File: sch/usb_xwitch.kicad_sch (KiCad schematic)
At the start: 82 parts, among them J1 USB3_A, J2 USB3_A, J3 USB3_A, J4 USB3_A, J5 USB3_A, J6 USB3_A, J7 Raspberry_Pi_2_3, J8 Conn_01x03, J9 Conn_02x03_Odd_Even, K1 J104D2C3VDC.15S, K2 J104D2C3VDC.15S, Q1 2N7002P, Q2 2N7002P, SW1 SW_MEC_5E, SW2 SW_MEC_5E, U1 Pico

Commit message: updated sch with correct lib
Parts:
- MUX1, MUX2: footprint USB_MUX_DEMUX_PI3USB302-A:USB_MUX_DEMUX_PI3USB302-A -> usb_xwitch:USB_MUX_DEMUX_PI3USB302-A
- U1: footprint RPi_Pico:RPi_Pico_SMD_TH -> usb_xwitch:RPi_Pico_SMD_TH
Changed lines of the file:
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@@
       (effects (font (size 1.27 1.27)) (justify left))
     )
-    (property "Footprint" "USB_MUX_DEMUX_PI3USB302-A:USB_MUX_DEMUX_PI3USB302-A" (id 2) (at 67.31 170.18 0)
+    (property "Footprint" "usb_xwitch:USB_MUX_DEMUX_PI3USB302-A" (id 2) (at 67.31 170.18 0)
       (effects (font (size 1.27 1.27)) hide)
     )
@@
       (effects (font (size 1.27 1.27)) (justify left))
     )
-    (property "Footprint" "USB_MUX_DEMUX_PI3USB302-A:USB_MUX_DEMUX_PI3USB302-A" (id 2) (at 139.7 62.23 0)
+    (property "Footprint" "usb_xwitch:USB_MUX_DEMUX_PI3USB302-A" (id 2) (at 139.7 62.23 0)
       (effects (font (size 1.27 1.27)) hide)
     )
@@
     (property "Reference" "U1" (id 0) (at 43.18 13.97 0))
     (property "Value" "Pico" (id 1) (at 43.18 16.51 0))
-    (property "Footprint" "RPi_Pico:RPi_Pico_SMD_TH" (id 2) (at 43.18 44.45 90)
+    (property "Footprint" "usb_xwitch:RPi_Pico_SMD_TH" (id 2) (at 43.18 44.45 90)
       (effects (font (size 1.27 1.27)) hide)
     )
@@
     )
     (path "/591ecbed-217e-48ed-ad79-2bef374432df"
-      (reference "MUX1") (unit 1) (value "PI3USB302-A") (footprint "USB_MUX_DEMUX_PI3USB302-A:USB_MUX_DEMUX_PI3USB302-A")
+      (reference "MUX1") (unit 1) (value "PI3USB302-A") (footprint "usb_xwitch:USB_MUX_DEMUX_PI3USB302-A")
     )
     (path "/32a0585d-b8a6-4ddd-ad0e-d8f7fa0d88f7"
-      (reference "MUX2") (unit 1) (value "PI3USB302-A") (footprint "USB_MUX_DEMUX_PI3USB302-A:USB_MUX_DEMUX_PI3USB302-A")
+      (reference "MUX2") (unit 1) (value "PI3USB302-A") (footprint "usb_xwitch:USB_MUX_DEMUX_PI3USB302-A")
     )
     (path "/01138bf6-010a-460b-9d5e-319df576379b"
@@
     )
     (path "/bb6a880b-1e04-4964-aba7-0ed014109109"
-      (reference "U1") (unit 1) (value "Pico") (footprint "RPi_Pico:RPi_Pico_SMD_TH")
-    )
-  )
+      (reference "U1") (unit 1) (value "Pico") (footprint "usb_xwitch:RPi_Pico_SMD_TH")
+    )
+  )

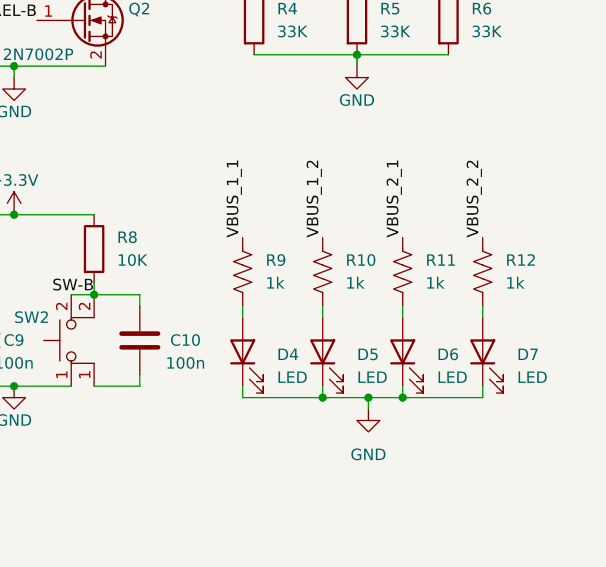
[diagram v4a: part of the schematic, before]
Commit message: updated led resistor value
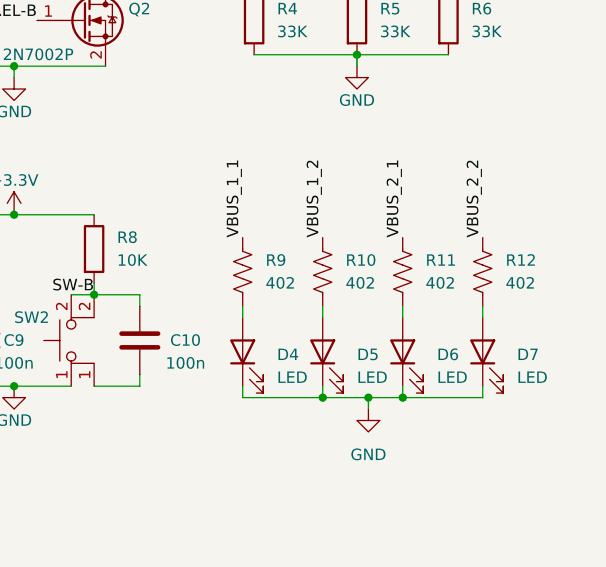
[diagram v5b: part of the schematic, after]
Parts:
- R10, R11, R12, R9: value 1k -> 402
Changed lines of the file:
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@@
       (effects (font (size 1.27 1.27)) (justify left))
     )
-    (property "Value" "1k" (id 1) (at 254 143.5099 0)
+    (property "Value" "402" (id 1) (at 254 143.5099 0)
       (effects (font (size 1.27 1.27)) (justify left))
     )
@@
       (effects (font (size 1.27 1.27)) (justify left))
     )
-    (property "Value" "1k" (id 1) (at 262.89 143.5099 0)
+    (property "Value" "402" (id 1) (at 262.89 143.5099 0)
       (effects (font (size 1.27 1.27)) (justify left))
     )
@@
       (effects (font (size 1.27 1.27)) (justify left))
     )
-    (property "Value" "1k" (id 1) (at 245.11 143.5099 0)
+    (property "Value" "402" (id 1) (at 245.11 143.5099 0)
       (effects (font (size 1.27 1.27)) (justify left))
     )
@@
       (effects (font (size 1.27 1.27)) (justify left))
     )
-    (property "Value" "1k" (id 1) (at 271.78 143.5099 0)
+    (property "Value" "402" (id 1) (at 271.78 143.5099 0)
       (effects (font (size 1.27 1.27)) (justify left))
     )
@@
     )
     (path "/ab7d4282-2b8b-4740-9065-f14f397a74b9"
-      (reference "R9") (unit 1) (value "1k") (footprint "Diode_SMD:D_0201_0603Metric_Pad0.64x0.40mm_HandSolder")
+      (reference "R9") (unit 1) (value "402") (footprint "Diode_SMD:D_0201_0603Metric_Pad0.64x0.40mm_HandSolder")
     )
     (path "/2077c3fe-878a-4115-9c7a-2c8d1e775f8e"
-      (reference "R10") (unit 1) (value "1k") (footprint "Diode_SMD:D_0201_0603Metric_Pad0.64x0.40mm_HandSolder")
+      (reference "R10") (unit 1) (value "402") (footprint "Diode_SMD:D_0201_0603Metric_Pad0.64x0.40mm_HandSolder")
     )
     (path "/61fa168a-7cd2-49f5-bf3a-d81e261300ae"
-      (reference "R11") (unit 1) (value "1k") (footprint "Diode_SMD:D_0201_0603Metric_Pad0.64x0.40mm_HandSolder")
+      (reference "R11") (unit 1) (value "402") (footprint "Diode_SMD:D_0201_0603Metric_Pad0.64x0.40mm_HandSolder")
     )
     (path "/ef6cee14-a255-4a4a-a342-1e947e99208d"
-      (reference "R12") (unit 1) (value "1k") (footprint "Diode_SMD:D_0201_0603Metric_Pad0.64x0.40mm_HandSolder")
+      (reference "R12") (unit 1) (value "402") (footprint "Diode_SMD:D_0201_0603Metric_Pad0.64x0.40mm_HandSolder")
     )
     (path "/e763556c-3aa8-4eb1-b263-7f108caa2254"

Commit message: updated pcb and sch
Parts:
- TP1, TP10, TP11, TP12, TP13, TP14, TP15, TP16, TP17, TP18, TP2, TP3, TP4, TP5, TP6, TP7, TP8, TP9: footprint TestPoint:TestPoint_Pad_D1.5mm -> TestPoint:TestPoint_Pad_D1.0mm

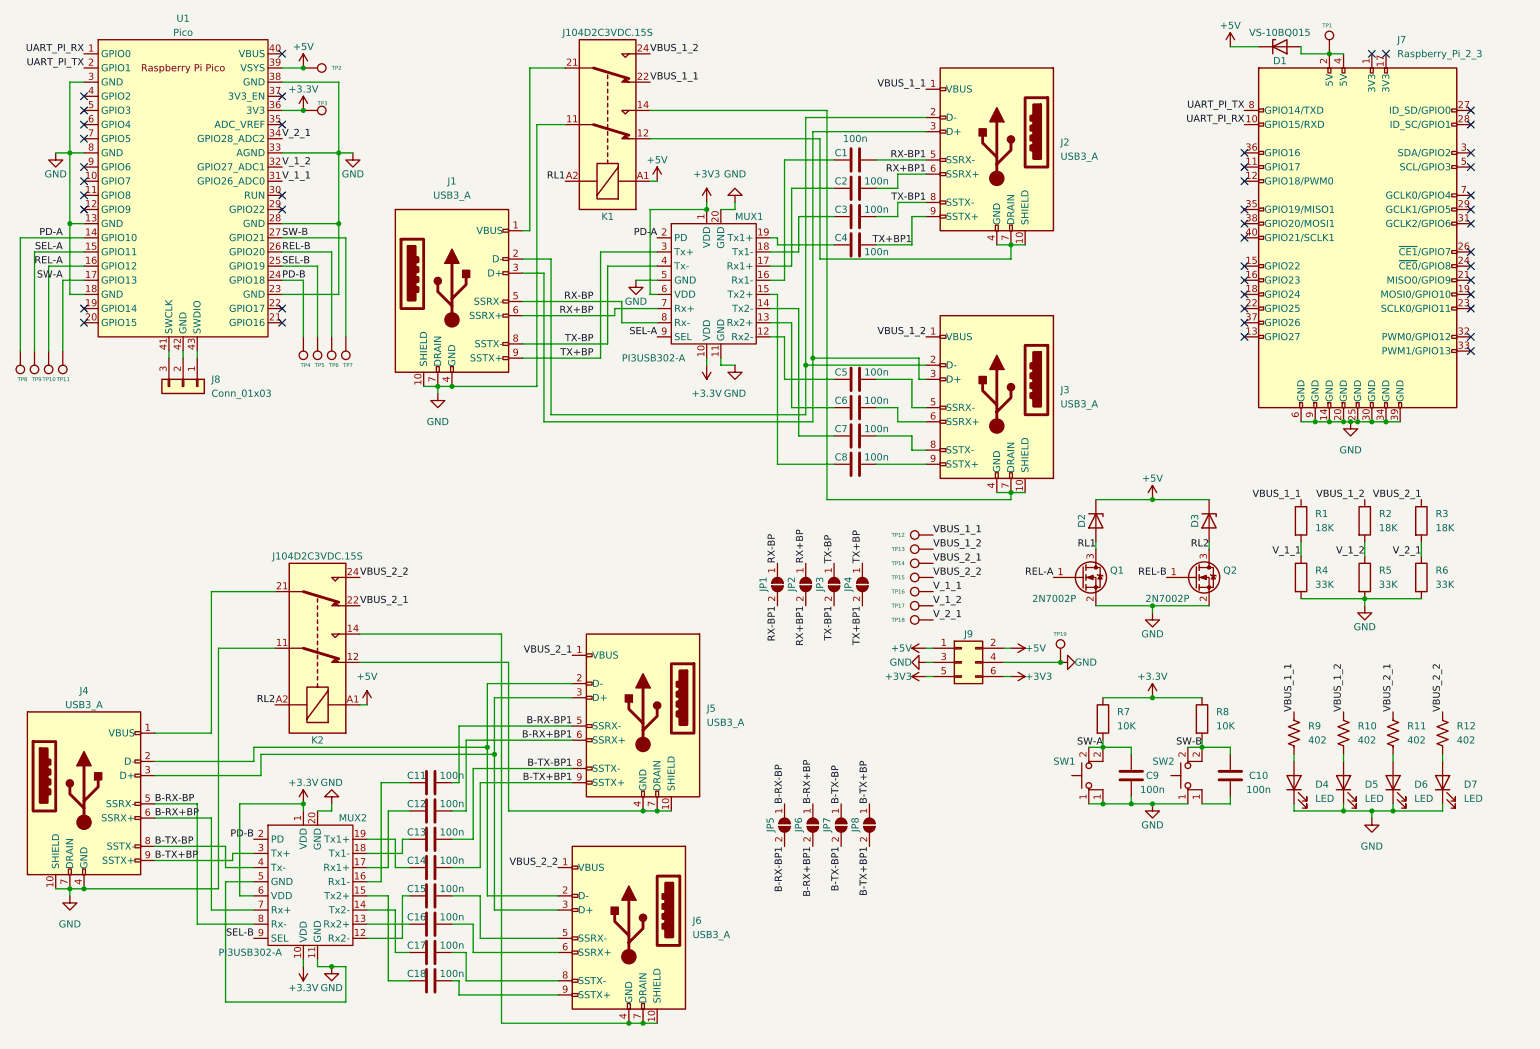
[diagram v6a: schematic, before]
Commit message: changing schematics with one less mux and one more power cycle channel
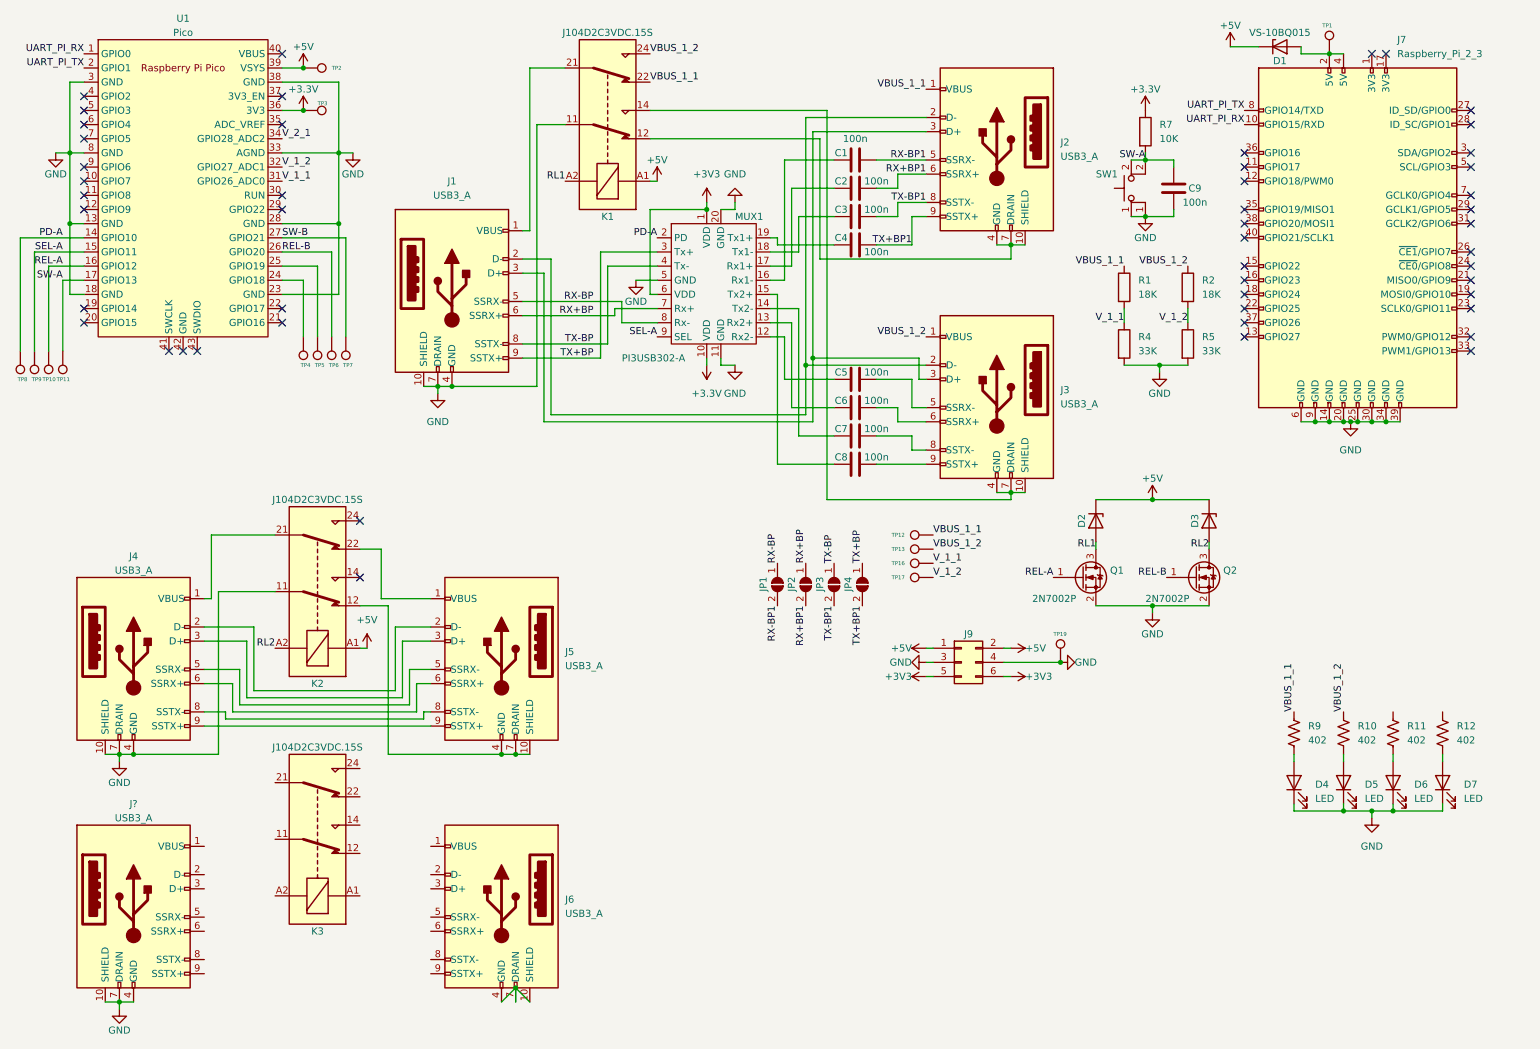
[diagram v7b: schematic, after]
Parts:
- removed C10, C11, C12, C13, C14, C15, C16, C17, C18: 100n, Capacitor_SMD:C_1206_3216Metric_Pad1.33x1.80mm_HandSolder, symbol Device:C
- removed J8: Conn_01x03, Connector_PinHeader_2.00mm:PinHeader_1x03_P2.00mm_Vertical, symbol Connector_Generic:Conn_01x03
- removed JP5, JP6, JP7, JP8: SolderJumper_2_Open, Jumper:SolderJumper-2_P1.3mm_Open_RoundedPad1.0x1.5mm, symbol Jumper:SolderJumper_2_Open
- removed MUX2: PI3USB302-A, usb_xwitch:USB_MUX_DEMUX_PI3USB302-A, symbol usb_xwitch:PI3USB302-A
- removed R3: 18K, Resistor_SMD:R_0805_2012Metric_Pad1.20x1.40mm_HandSolder, symbol Device:R
- removed R6: 33K, Resistor_SMD:R_0805_2012Metric_Pad1.20x1.40mm_HandSolder, symbol Device:R
- removed R8: 10K, Resistor_SMD:R_0603_1608Metric_Pad0.98x0.95mm_HandSolder, symbol Device:R
- removed SW2: SW_MEC_5E, Button_Switch_THT:SW_PUSH-12mm, symbol Switch:SW_MEC_5E
- removed TP14, TP15, TP18: TestPoint, TestPoint:TestPoint_Pad_D1.0mm, symbol Connector:TestPoint
- added J?: USB3_A, usb_xwitch:USB3_A_AdamTech_USB-A3-S-RA, symbol Connector:USB3_A
- added K3: J104D2C3VDC.15S, usb_xwitch:J104D2C3VDC.15S, symbol usb_xwitch:J104D2C3VDC.15S
- SW1: footprint Button_Switch_THT:SW_PUSH-12mm -> Button_Switch_THT:SW_PUSH_6mm
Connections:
- net B-RX+BP1 is gone; now on an unnamed net: J5.6 (SSRX+)
- net B-RX-BP1 is gone; now on an unnamed net: J5.5 (SSRX-)
- net B-TX+BP1 is gone; now on an unnamed net: J5.9 (SSTX+)
- net B-TX-BP1 is gone; now on an unnamed net: J5.8 (SSTX-)
- net GND: now also J?.10 (SHIELD), J?.4 (GND), J?.7 (DRAIN)
- net at J6.10 (SHIELD), J6.4 (GND), J6.7 (DRAIN): no longer K2.14
- net at J4.2 (D-), J5.2 (D-): no longer J6.2 (D-)
- net at J4.3 (D+), J5.3 (D+): no longer J6.3 (D+)
- net B-RX+BP: no longer names the net of J4.6 (SSRX+)
- net B-RX-BP: no longer names the net of J4.5 (SSRX-)
- net B-TX+BP: no longer names the net of J4.9 (SSTX+)
- net B-TX-BP: no longer names the net of J4.8 (SSTX-)
- net PD-B: no longer names the net of TP4.1, U1.24 (GPIO18)
- net SEL-B: no longer names the net of TP5.1, U1.25 (GPIO19)
- net VBUS_2_1: no longer names the net of J5.1 (VBUS), K2.22
- net VBUS_2_1: no longer R11.1
- removed net VBUS_2_2: J6.1 (VBUS), K2.24, R12.1
- no-connect marks 45 -> 50
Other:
- moved on the sheet: C9, J4, J5, J6, K2, R1, R2, R4, R5, R7, SW1, TP16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

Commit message: updated rpi connector, pico footprint and board dimension
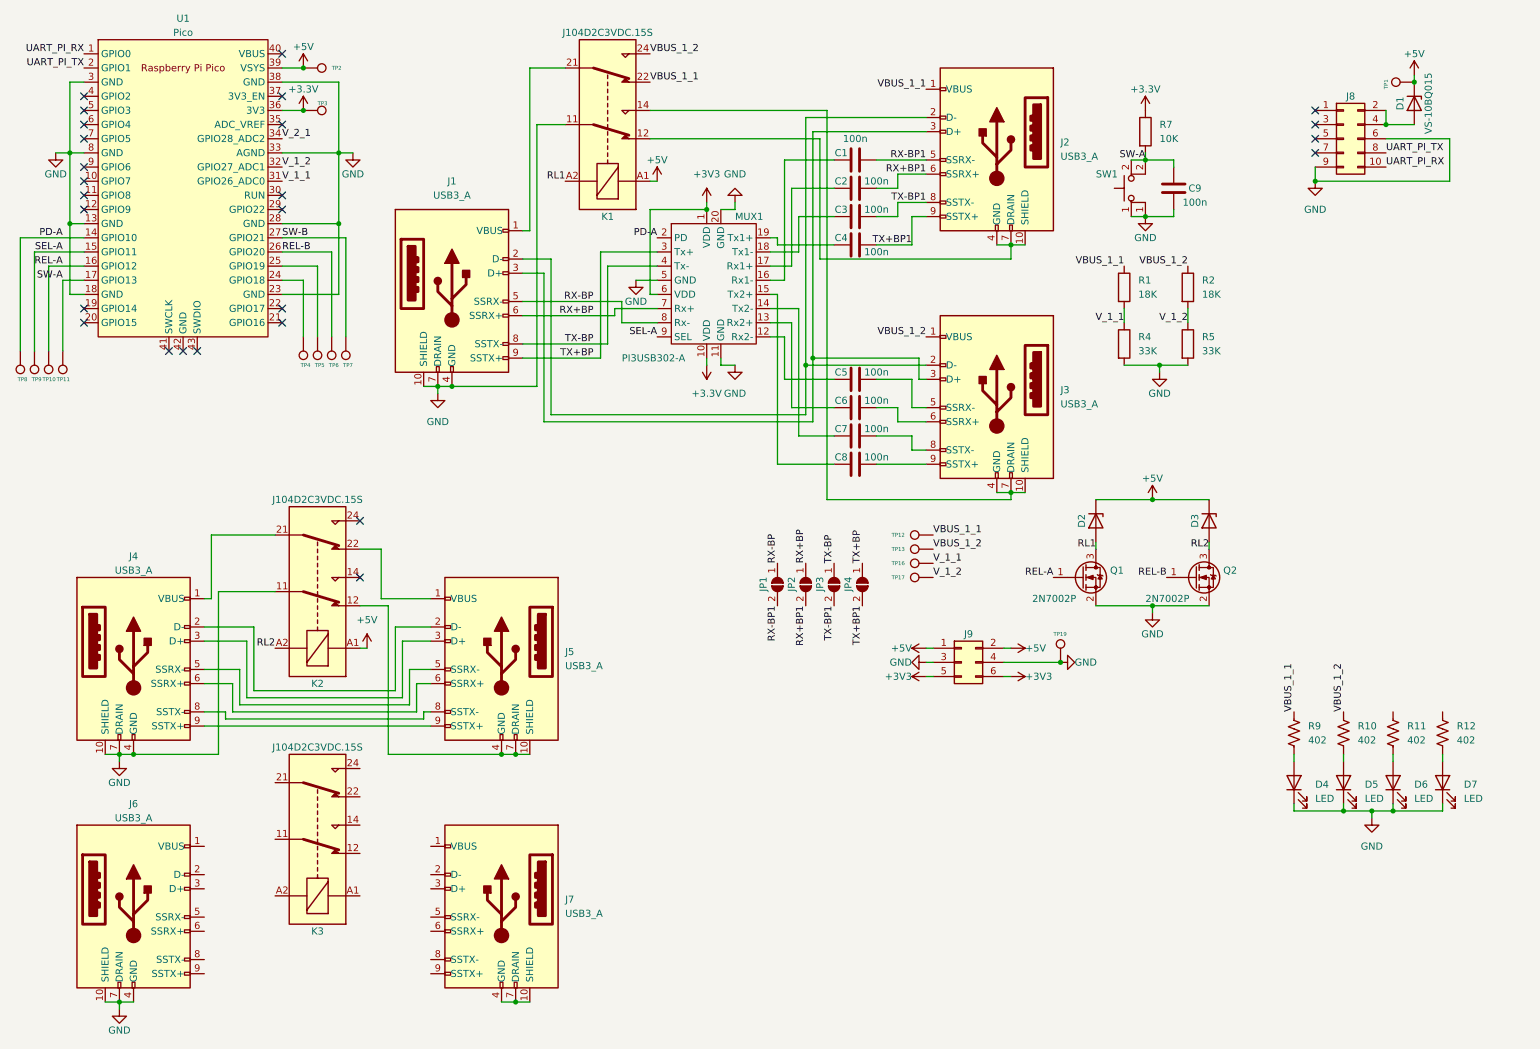
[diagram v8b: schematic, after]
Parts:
- removed J7: Raspberry_Pi_2_3, Connector_PinSocket_2.54mm:PinSocket_2x20_P2.54mm_Vertical, symbol Connector:Raspberry_Pi_2_3
- added J8: Conn_02x05_Odd_Even, Connector_PinSocket_2.54mm:PinSocket_2x05_P2.54mm_Vertical, symbol Connector_Generic:Conn_02x05_Odd_Even
- U1: footprint usb_xwitch:RPi_Pico_SMD_TH -> usb_xwitch:RPi_Pico_SMD
- gave numbers to parts that had none: 1
- renumbered J6 to J7
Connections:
- net +5V: now also TP1.1
- net GND: now also J8.6 (Pin_6), J8.9 (Pin_9)
- net UART_PI_RX: now also J8.10 (Pin_10)
- net UART_PI_TX: now also J8.8 (Pin_8)
- net at D1.2 (A): now also J8.2 (Pin_2), J8.4 (Pin_4); no longer TP1.1
- no-connect marks 50 -> 26
